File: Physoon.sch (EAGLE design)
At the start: 37 parts, among them IC2 74AHC1G125DBV, IC3 74AHC1G125DBV, M1 HX1, X1 BU-SMA-V

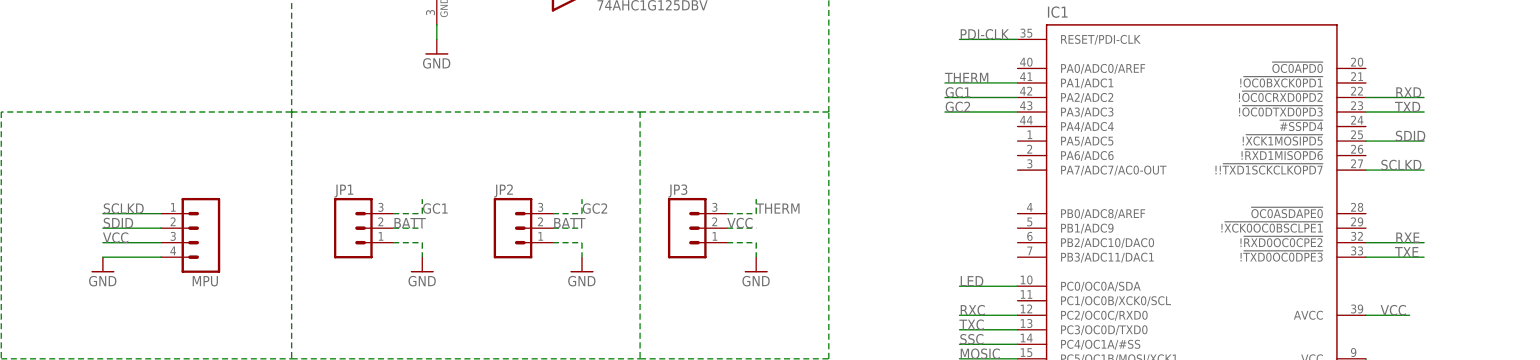
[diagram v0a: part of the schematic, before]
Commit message: fix interface for IMU
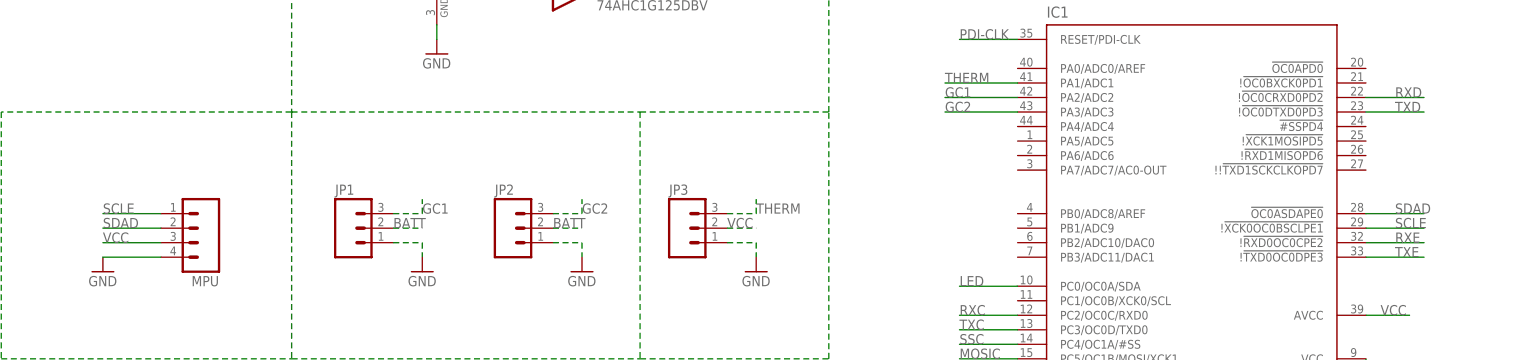
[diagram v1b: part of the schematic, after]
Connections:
- removed net SCLKD: IC1.!!!TXD1SCKCLKOPD7, MPU.1
- removed net SDID: IC1.!!XCK1MOSIPD5, MPU.2
- new net SCLE: IC1.!!XCK0OC0BSCLPE1, MPU.1
- new net SDAD: IC1.!OC0ASDAPE0, MPU.2
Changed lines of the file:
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@@
 <?xml version="1.0" encoding="utf-8"?>
 <!DOCTYPE eagle SYSTEM "eagle.dtd">
-<eagle version="8.1.1">
+<eagle version="8.2.0">
 <drawing>
 <settings>
@@
 </segment>
 </net>
-<net name="SDID" class="0">
-<segment>
-<pinref part="IC1" gate="G$1" pin="!!XCK1MOSIPD5"/>
-<wire x1="109.22" y1="88.9" x2="119.38" y2="88.9" width="0.1524" layer="91"/>
-<label x="114.3" y="88.9" size="1.778" layer="95"/>
-</segment>
-<segment>
-<pinref part="MPU" gate="G$1" pin="2"/>
-<wire x1="-101.6" y1="73.66" x2="-111.76" y2="73.66" width="0.1524" layer="91"/>
-<label x="-111.76" y="73.66" size="1.778" layer="95"/>
-</segment>
-</net>
-<net name="SCLKD" class="0">
-<segment>
-<pinref part="IC1" gate="G$1" pin="!!!TXD1SCKCLKOPD7"/>
-<wire x1="109.22" y1="83.82" x2="119.38" y2="83.82" width="0.1524" layer="91"/>
-<label x="111.76" y="83.82" size="1.778" layer="95"/>
-</segment>
+<net name="SCLE" class="0">
 <segment>
 <pinref part="MPU" gate="G$1" pin="1"/>
 <wire x1="-101.6" y1="76.2" x2="-111.76" y2="76.2" width="0.1524" layer="91"/>
 <label x="-111.76" y="76.2" size="1.778" layer="95"/>
+</segment>
+<segment>
+<pinref part="IC1" gate="G$1" pin="!!XCK0OC0BSCLPE1"/>
+<wire x1="109.22" y1="73.66" x2="119.38" y2="73.66" width="0.1524" layer="91"/>
+<label x="114.3" y="73.66" size="1.778" layer="95"/>
 </segment>
 </net>
@@
 </segment>
 </net>
+<net name="SDAD" class="0">
+<segment>
+<pinref part="MPU" gate="G$1" pin="2"/>
+<wire x1="-101.6" y1="73.66" x2="-111.76" y2="73.66" width="0.1524" layer="91"/>
+<label x="-111.76" y="73.66" size="1.778" layer="95"/>
+</segment>
+<segment>
+<pinref part="IC1" gate="G$1" pin="!OC0ASDAPE0"/>
+<wire x1="109.22" y1="76.2" x2="119.38" y2="76.2" width="0.1524" layer="91"/>
+<label x="114.3" y="76.2" size="1.778" layer="95"/>
+</segment>
+</net>
